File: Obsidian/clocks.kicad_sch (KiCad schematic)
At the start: 48 parts, among them J16 Conn_Coaxial, Q7 BSS138LT1G, U13 SI5340B-D-GM, U3 Si5351A-B-GT, Y1 KC2520Z25.0000C1KX00, Y2 XTAL_48MHZ_KYOCERA_CX3225SB48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, Y6 XTAL_25MHZ_TXC_8Y-25.000MAAJ-T

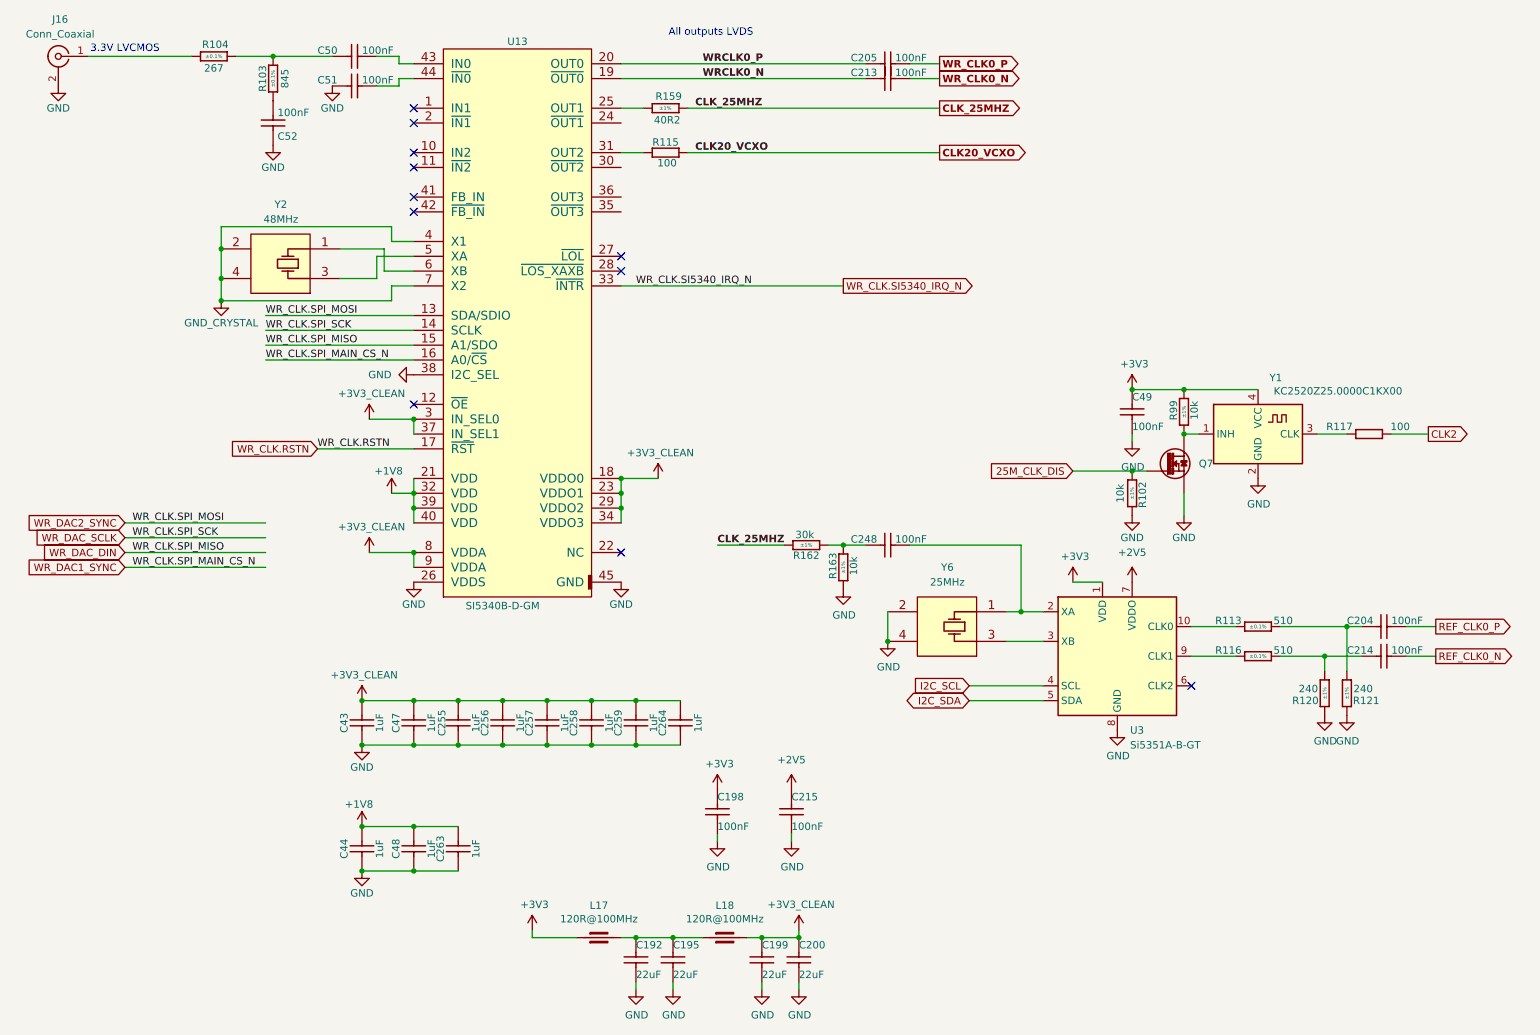
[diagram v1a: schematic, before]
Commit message: new font; removed clk gen; added resistors for 2 PMODs
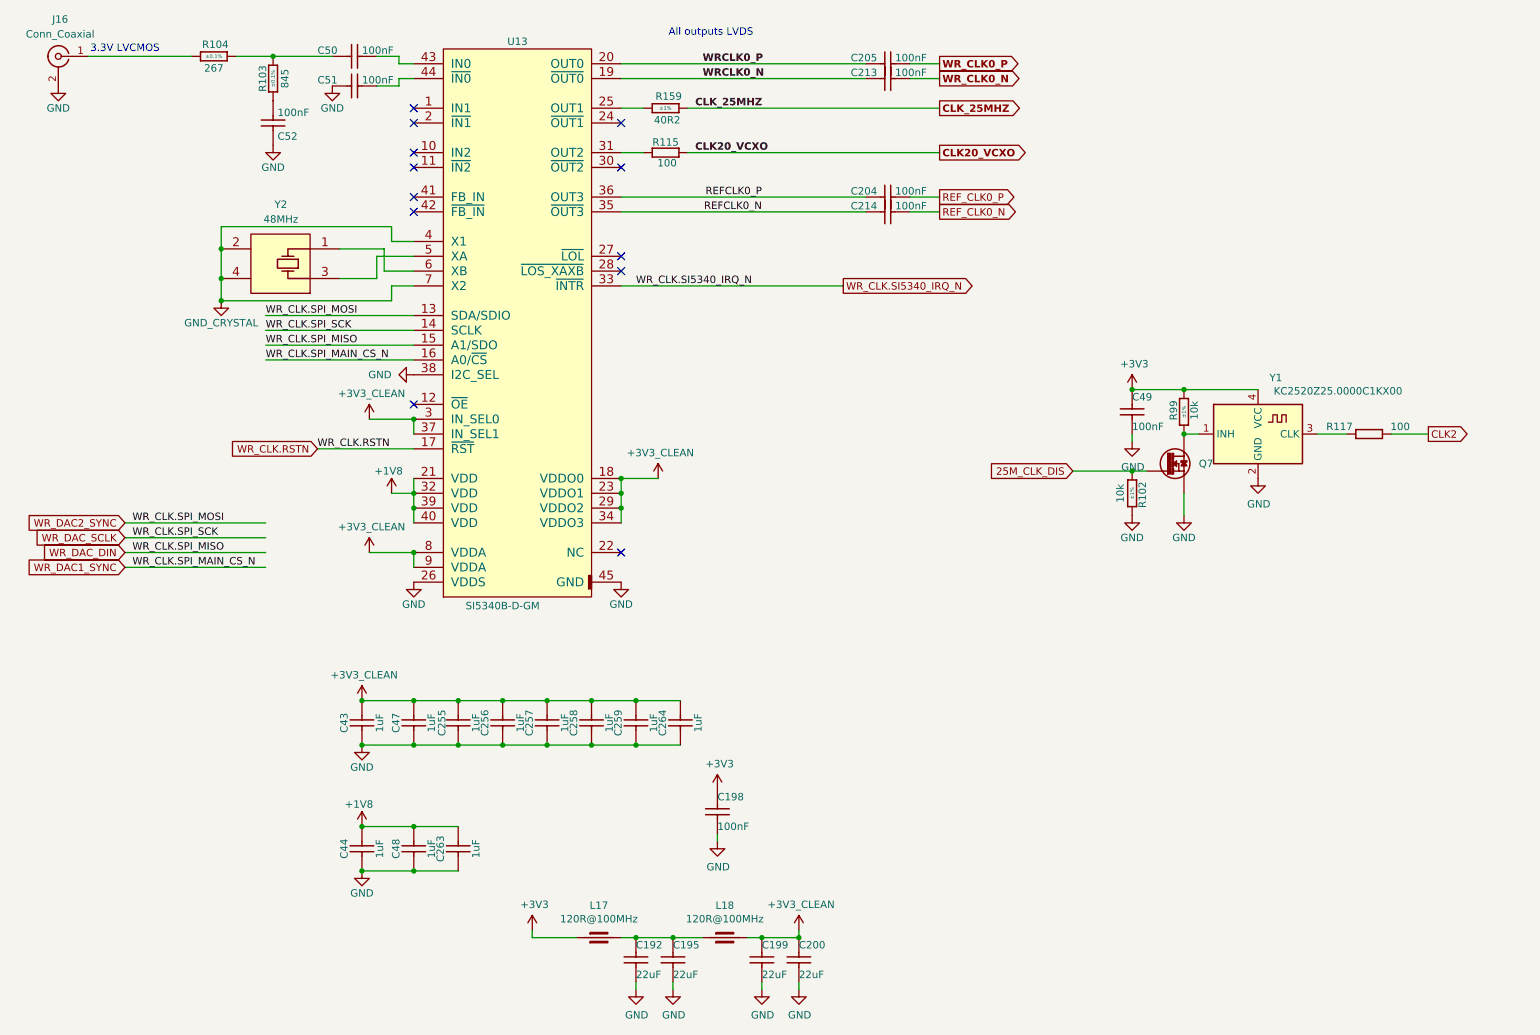
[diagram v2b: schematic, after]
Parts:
- removed C215: CC0201_100NF_6.3V_10%_X5R, Capacitors SMD:CAPC0603X33N, symbol Capacitors_SMD:CC0201_100NF_6.3V_10%_X5R
- removed C248: CC0402_100NF_50V_10%_X7R, Capacitors SMD:CAPC1005X55N, symbol Capacitors SMD:CC0402_100NF_50V_10%_X7R
- removed R113, R116: R0402_510R_0.1%_0.0625W_10PPM, Resistors SMD:RESC1005X40N, symbol Resistors SMD:R0402_510R_0.1%_0.0625W_10PPM
- removed R120, R121: R0402_240R_1%_0.0625W_100PPM, Resistors SMD:RESC1005X40N, symbol Resistors SMD:R0402_240R_1%_0.0625W_100PPM
- removed R162: R0402_30K_1%_0.0625W_100PPM, Resistors SMD:RESC1005X40N, symbol Resistors SMD:R0402_30K_1%_0.0625W_100PPM
- removed R163: R0402_10K_1%_0.0625W_100PPM, Resistors SMD:RESC1005X40N, symbol Resistors SMD:R0402_10K_1%_0.0625W_100PPM
- removed U3: Si5351A-B-GT, Package_SO:MSOP-10_3x3mm_P0.5mm, symbol Oscillator:Si5351A-B-GT
- removed Y6: XTAL_25MHZ_TXC_8Y-25.000MAAJ-T, ICs And Semiconductors SMD:XTAL_TXC_8Y, symbol Crystals & Oscillators:XTAL_25MHZ_TXC_8Y-25.000MAAJ-T
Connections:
- net REFCLK0_N: now reaches C214.2
- net REFCLK0_N: now also U13.35 (~{OUT3})
- net REFCLK0_P: now reaches C204.2
- net REFCLK0_P: now also U13.36 (OUT3)
- no-connect marks 11 -> 12
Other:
- moved on the sheet: C204, C214

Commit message: ready to manufacture
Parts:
- removed C198: CC0201_100NF_6.3V_10%_X5R, Capacitors SMD:CAPC0603X33N, symbol Capacitors_SMD:CC0201_100NF_6.3V_10%_X5R
